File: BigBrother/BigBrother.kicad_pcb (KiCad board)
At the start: 2 copper layers, 67 x 71 mm, 4 parts, among them J1 RPi_GPIO, U1 bno055, U2 BMP388, U3 VHN5019_Breakout

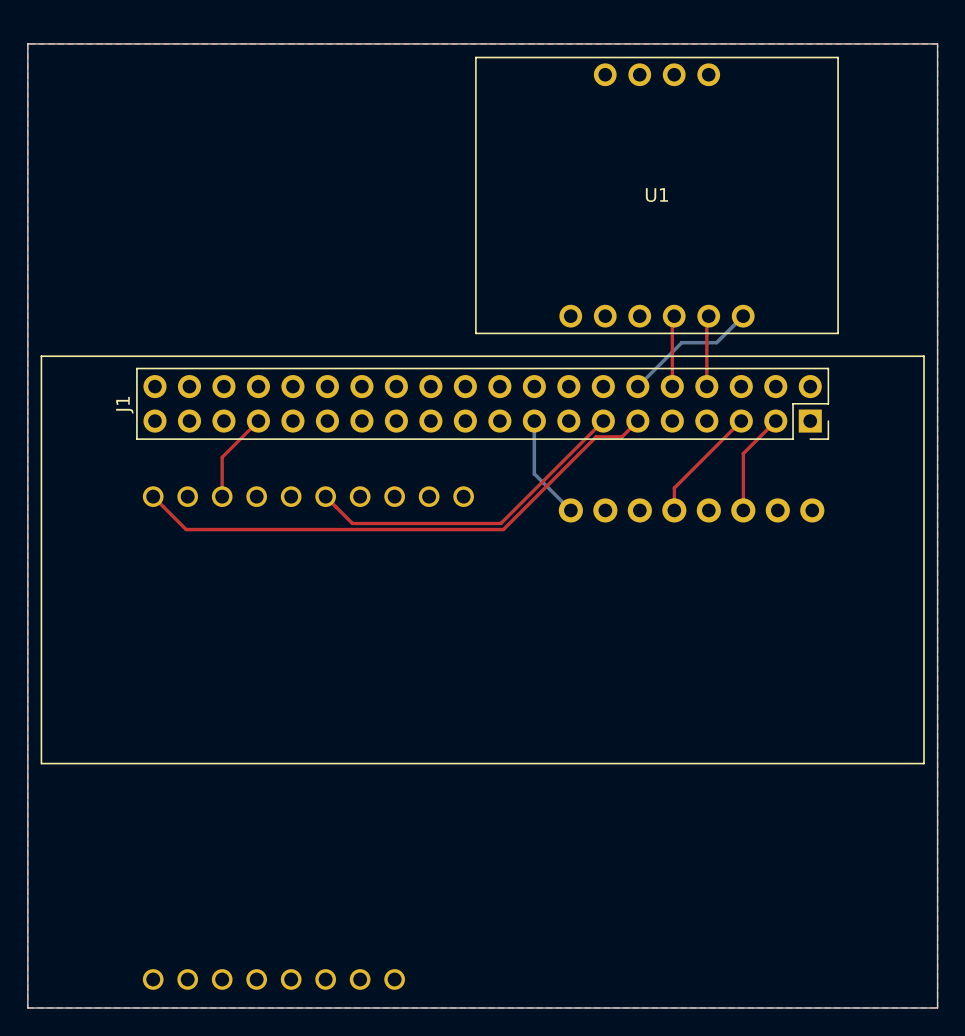
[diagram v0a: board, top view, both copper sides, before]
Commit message: Mounting holes
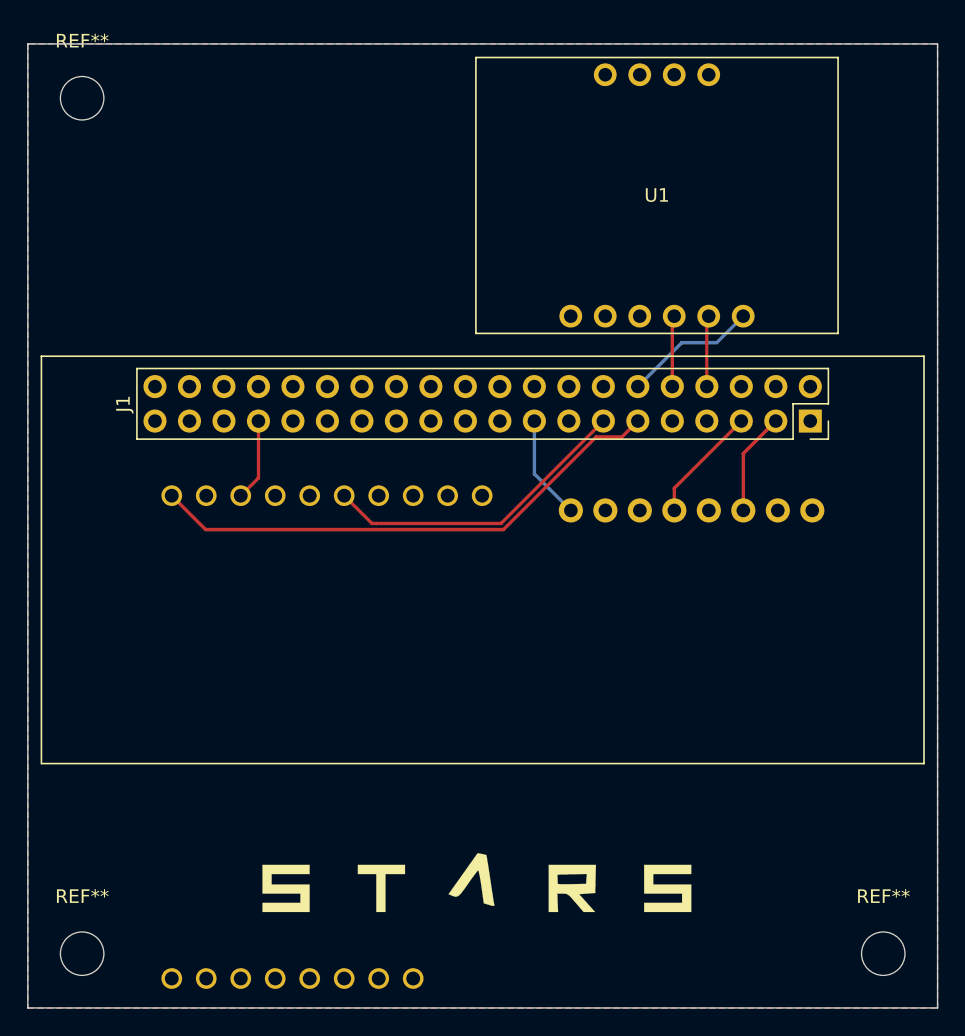
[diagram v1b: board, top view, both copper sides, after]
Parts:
- added G***: LOGO, NUSTARS:logo, F.Cu at (138.0, 118.0)
- added REF**: MountingHole_3.2mm_M3, MountingHole:MountingHole_3.2mm_M3, F.Cu at (116.0, 122.0)
- added REF**: MountingHole_3.2mm_M3, MountingHole:MountingHole_3.2mm_M3, F.Cu at (175.0, 122.0)
- added REF**: MountingHole_3.2mm_M3, MountingHole:MountingHole_3.2mm_M3, F.Cu at (116.0, 59.0)
- moved U3 1.37 mm to (148.0, 87.0)
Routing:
- net GPIO_INB: track 24.4 -> 23.1 mm
- net GPIO_INA: track 40.0 -> 38.7 mm
- net GPIO_PWM: track 6.67 -> 6.04 mm
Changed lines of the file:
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@@
     (tracks 26)
     (zones 0)
-    (modules 4)
+    (modules 8)
     (nets 50)
   )
   (page A4)
   (layers
-    (0 F.Cu signal)
-    (31 B.Cu signal)
+    (0 F.Cu signal hide)
+    (31 B.Cu signal hide)
     (32 B.Adhes user)
     (33 F.Adhes user)
@@
     (add_net TXD)
   )
+  (module MountingHole:MountingHole_3.2mm_M3 (layer F.Cu)
+    (at 116 122)
+    (descr "Mounting Hole 3.2mm, no annular, M3")
+    (tags "mounting hole 3.2mm no annular m3")
+    (attr virtual)
+    (fp_text reference REF** (at 0 -4.2) (layer F.SilkS)
+      (effects (font (size 1 1) (thickness 0.15)))
+    )
+    (fp_text value MountingHole_3.2mm_M3 (at 0 4.2) (layer F.Fab)
+      (effects (font (size 1 1) (thickness 0.15)))
+    )
+    (fp_circle (center 0 0) (end 3.45 0) (layer F.CrtYd) (width 0.05))
+    (fp_circle (center 0 0) (end 3.2 0) (layer Cmts.User) (width 0.15))
+    (fp_text user %R (at 0.3 0) (layer F.Fab)
+      (effects (font (size 1 1) (thickness 0.15)))
+    )
+    (pad 1 np_thru_hole circle (at 0 0) (size 3.2 3.2) (drill 3.2) (layers *.Cu *.Mask))
+  )
+  (module MountingHole:MountingHole_3.2mm_M3 (layer F.Cu)
+    (at 175 122)
+    (descr "Mounting Hole 3.2mm, no annular, M3")
+    (tags "mounting hole 3.2mm no annular m3")
+    (attr virtual)
+    (fp_text reference REF** (at 0 -4.2) (layer F.SilkS)
+      (effects (font (size 1 1) (thickness 0.15)))
+    )
+    (fp_text value MountingHole_3.2mm_M3 (at 0 4.2) (layer F.Fab)
+      (effects (font (size 1 1) (thickness 0.15)))
+    )
+    (fp_circle (center 0 0) (end 3.45 0) (layer F.CrtYd) (width 0.05))
+    (fp_circle (center 0 0) (end 3.2 0) (layer Cmts.User) (width 0.15))
+    (fp_text user %R (at 0.3 0) (layer F.Fab)
+      (effects (font (size 1 1) (thickness 0.15)))
+    )
+    (pad 1 np_thru_hole circle (at 0 0) (size 3.2 3.2) (drill 3.2) (layers *.Cu *.Mask))
+  )
+  (module MountingHole:MountingHole_3.2mm_M3 (layer F.Cu)
+    (at 116 59)
+    (descr "Mounting Hole 3.2mm, no annular, M3")
+    (tags "mounting hole 3.2mm no annular m3")
+    (attr virtual)
+    (fp_text reference REF** (at 0 -4.2) (layer F.SilkS)
+      (effects (font (size 1 1) (thickness 0.15)))
+    )
+    (fp_text value MountingHole_3.2mm_M3 (at 0 4.2) (layer F.Fab)
+      (effects (font (size 1 1) (thickness 0.15)))
+    )
+    (fp_circle (center 0 0) (end 3.45 0) (layer F.CrtYd) (width 0.05))
+    (fp_circle (center 0 0) (end 3.2 0) (layer Cmts.User) (width 0.15))
+    (fp_text user %R (at 0.3 0) (layer F.Fab)
+      (effects (font (size 1 1) (thickness 0.15)))
+    )
+    (pad 1 np_thru_hole circle (at 0 0) (size 3.2 3.2) (drill 3.2) (layers *.Cu *.Mask))
+  )
+  (module NUSTARS:logo (layer F.Cu)
+    (at 138 118)
+    (fp_text reference G*** (at 0 0) (layer F.SilkS) hide
+      (effects (font (size 1.524 1.524) (thickness 0.3)))
+    )
+    (fp_text value LOGO (at 0.75 0) (layer F.SilkS) hide
+      (effects (font (size 1.524 1.524) (thickness 0.3)))
+    )
+    (fp_poly (pts (xy -5.249334 -1.862667) (xy -8.043334 -1.862667) (xy -8.043334 -1.100667) (xy -5.249334 -1.100667)
+      (xy -5.249334 0.931333) (xy -8.720667 0.931333) (xy -8.720667 0.254) (xy -5.926667 0.254)
+      (xy -5.926667 -0.423334) (xy -8.720667 -0.423334) (xy -8.720667 -2.54) (xy -5.249334 -2.54)
+      (xy -5.249334 -1.862667)) (layer F.SilkS) (width 0.01))
+    (fp_poly (pts (xy 1.778 -1.862667) (xy 0.338666 -1.862667) (xy 0.338666 0.931333) (xy -0.338667 0.931333)
+      (xy -0.338667 -1.862667) (xy -1.693334 -1.862667) (xy -1.693334 -2.54) (xy 1.778 -2.54)
+      (xy 1.778 -1.862667)) (layer F.SilkS) (width 0.01))
+    (fp_poly (pts (xy 15.814105 -1.502834) (xy 15.790333 -0.465667) (xy 15.197666 -0.423334) (xy 14.605 -0.381)
+      (xy 14.982433 0.042333) (xy 15.215797 0.303674) (xy 15.436851 0.550568) (xy 15.569774 0.6985)
+      (xy 15.77968 0.931333) (xy 14.929303 0.931333) (xy 14.351 0.254) (xy 14.09024 -0.047934)
+      (xy 13.905571 -0.243455) (xy 13.764015 -0.35568) (xy 13.632596 -0.407727) (xy 13.478337 -0.422714)
+      (xy 13.384514 -0.423533) (xy 12.996333 -0.423732) (xy 13.023947 0.253801) (xy 13.05156 0.931333)
+      (xy 12.361333 0.931333) (xy 12.361333 -1.820334) (xy 13.01021 -1.820334) (xy 13.017382 -1.502834)
+      (xy 13.023772 -1.285002) (xy 13.030416 -1.151357) (xy 13.031611 -1.140395) (xy 13.113654 -1.125021)
+      (xy 13.332286 -1.115826) (xy 13.654852 -1.113472) (xy 14.048697 -1.118621) (xy 14.075833 -1.119228)
+      (xy 15.113 -1.143) (xy 15.13916 -1.505401) (xy 15.16532 -1.867801) (xy 14.087765 -1.844067)
+      (xy 13.01021 -1.820334) (xy 12.361333 -1.820334) (xy 12.361333 -2.54) (xy 15.837878 -2.54)
+      (xy 15.814105 -1.502834)) (layer F.SilkS) (width 0.01))
+    (fp_poly (pts (xy 22.86 -1.862667) (xy 20.066 -1.862667) (xy 20.066 -1.100667) (xy 22.86 -1.100667)
+      (xy 22.86 0.931333) (xy 19.388666 0.931333) (xy 19.388666 0.254) (xy 22.182666 0.254)
+      (xy 22.182666 -0.423334) (xy 19.388666 -0.423334) (xy 19.388666 -2.54) (xy 22.86 -2.54)
+      (xy 22.86 -1.862667)) (layer F.SilkS) (width 0.01))
+    (fp_poly (pts (xy 7.436885 -3.34482) (xy 7.644768 -3.301111) (xy 7.764359 -3.266712) (xy 7.77241 -3.261983)
+      (xy 7.791942 -3.174539) (xy 7.831671 -2.945047) (xy 7.887495 -2.599044) (xy 7.955314 -2.162062)
+      (xy 8.031027 -1.659638) (xy 8.046536 -1.555034) (xy 8.125093 -1.029282) (xy 8.198057 -0.551216)
+      (xy 8.260887 -0.149793) (xy 8.309042 0.146032) (xy 8.337978 0.307302) (xy 8.340239 0.3175)
+      (xy 8.361118 0.437074) (xy 8.327181 0.487525) (xy 8.204208 0.474957) (xy 7.957978 0.405472)
+      (xy 7.916687 0.393046) (xy 7.578374 0.291106) (xy 7.407969 -0.933947) (xy 7.343476 -1.364272)
+      (xy 7.280373 -1.726207) (xy 7.224408 -1.990826) (xy 7.874 -0.254) (xy 7.167838 -2.14262)
+      (xy 7.097066 -2.070521) (xy 6.950693 -1.883843) (xy 6.747949 -1.608292) (xy 6.508067 -1.269579)
+      (xy 6.423663 -1.147787) (xy 6.13946 -0.741534) (xy 5.925127 -0.459995) (xy 5.757481 -0.286408)
+      (xy 5.613341 -0.204011) (xy 5.469526 -0.196044) (xy 5.302854 -0.245743) (xy 5.222184 -0.279044)
+      (xy 4.983369 -0.381116) (xy 6.05507 -1.891929) (xy 7.126771 -3.402741) (xy 7.436885 -3.34482)) (layer F.SilkS) (width 0.01))
+  )
   (module "Raspberry Pi Zero:RPI_Zero" (layer F.Cu)
     (at 113 78)
@@
   )
   (module NUSTARS:VNH5019_breakout (layer B.Cu)
-    (at 146.6342 87.0712 180)
+    (at 148 87 180)
     (fp_text reference U3 (at 22.86 -19.05) (layer B.SilkS)
       (effects (font (size 1 1) (thickness 0.15)) (justify mirror))
@@
   (segment (start 159.465 75.19) (end 159.605 75.05) (width 0.25) (layer F.Cu) (net 9))
   (segment (start 159.465 80.235) (end 159.465 75.19) (width 0.25) (layer F.Cu) (net 9))
-  (segment (start 121.996199 89.103199) (end 121.2342 88.3412) (width 0.25) (layer F.Cu) (net 10))
-  (segment (start 123.66002 90.76702) (end 121.996199 89.103199) (width 0.25) (layer F.Cu) (net 10))
-  (segment (start 147.02939 90.76702) (end 123.66002 90.76702) (width 0.25) (layer F.Cu) (net 10))
   (segment (start 153.846409 83.950001) (end 147.02939 90.76702) (width 0.25) (layer F.Cu) (net 10))
   (segment (start 155.749999 83.950001) (end 153.846409 83.950001) (width 0.25) (layer F.Cu) (net 10))
   (segment (start 156.925 82.775) (end 155.749999 83.950001) (width 0.25) (layer F.Cu) (net 10))
+  (segment (start 125.09702 90.76702) (end 125.23298 90.76702) (width 0.25) (layer F.Cu) (net 10))
+  (segment (start 122.6 88.27) (end 125.09702 90.76702) (width 0.25) (layer F.Cu) (net 10))
+  (segment (start 147.02939 90.76702) (end 125.23298 90.76702) (width 0.25) (layer F.Cu) (net 10))
   (segment (start 154.385 82.775) (end 146.84299 90.31701) (width 0.25) (layer F.Cu) (net 11))
-  (segment (start 146.84299 90.31701) (end 135.91001 90.31701) (width 0.25) (layer F.Cu) (net 11))
-  (segment (start 134.696199 89.103199) (end 133.9342 88.3412) (width 0.25) (layer F.Cu) (net 11))
-  (segment (start 135.91001 90.31701) (end 134.696199 89.103199) (width 0.25) (layer F.Cu) (net 11))
-  (segment (start 126.3142 85.4458) (end 128.985 82.775) (width 0.25) (layer F.Cu) (net 26))
-  (segment (start 126.3142 88.3412) (end 126.3142 85.4458) (width 0.25) (layer F.Cu) (net 26))
+  (segment (start 137.34701 90.31701) (end 137.68299 90.31701) (width 0.25) (layer F.Cu) (net 11))
+  (segment (start 135.3 88.27) (end 137.34701 90.31701) (width 0.25) (layer F.Cu) (net 11))
+  (segment (start 146.84299 90.31701) (end 137.68299 90.31701) (width 0.25) (layer F.Cu) (net 11))
+  (segment (start 128.985 86.965) (end 128.985 82.775) (width 0.25) (layer F.Cu) (net 26))
+  (segment (start 127.68 88.27) (end 128.985 86.965) (width 0.25) (layer F.Cu) (net 26))
   (segment (start 156.925 80.235) (end 160.16 77) (width 0.25) (layer B.Cu) (net 49))
   (segment (start 162.735 77) (end 164.685 75.05) (width 0.25) (layer B.Cu) (net 49))
